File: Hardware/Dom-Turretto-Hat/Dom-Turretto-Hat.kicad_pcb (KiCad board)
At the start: 2 copper layers, 65 x 56 mm, 54 parts, among them J1 Raspberry_Pi_2_3, J2 Conn_Coaxial, J3 Barrel_Jack_Switch, J4 Conn_01x02, U1 CAT24C32WI-GT3, U2 MAX-M8Q, U3 LM22679TJ-5.0/NOPB, U4 LTC4451AV#TRMPBF, U5 LTC4451AV#TRMPBF, U6 LT1963AxST-3.3, U7 LTC4411ES5TRMPBF

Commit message: Fix XT60 connector
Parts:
- J4: footprint Connector_AMASS:AMASS_XT60-F_1x02_P7.20mm_Vertical -> Connector_AMASS:AMASS_XT60-M_1x02_P7.20mm_Vertical
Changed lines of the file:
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@@
     )
   )
-  (footprint "Connector_AMASS:AMASS_XT60-F_1x02_P7.20mm_Vertical" (layer "F.Cu")
+  (footprint "Connector_AMASS:AMASS_XT60-M_1x02_P7.20mm_Vertical" (layer "F.Cu")
     (at 151.5 121.9 -90)
     (descr "AMASS female XT60, through hole, vertical, https://www.tme.eu/Document/2d152ced3b7a446066e6c419d84bb460/XT60%20SPEC.pdf")
@@
       (effects (font (size 1 1) (thickness 0.15)))
     )
-    (fp_text value "Conn_01x02" (at 3.6 5.4 90) (layer "F.Fab")
+    (fp_text value "Conn_01x02" (at 3.6 5.4 -90) (layer "F.Fab")
       (effects (font (size 1 1) (thickness 0.15)))
     )
-    (fp_text user "${REFERENCE}" (at 3.6 0.05 90) (layer "F.Fab")
+    (fp_text user "${REFERENCE}" (at 3.6 0.05 -90) (layer "F.Fab")
       (effects (font (size 1 1) (thickness 0.15)))
     )
-    (fp_line (start 11.45 4.15) (end 11.45 -4.15) (layer "F.SilkS") (width 0.12))
-    (fp_line (start -1.4 -4.15) (end -4.25 -1.6) (layer "F.SilkS") (width 0.12))
-    (fp_line (start -4.25 -1.6) (end -4.25 1.55) (layer "F.SilkS") (width 0.12))
     (fp_line (start -1.4 4.15) (end 11.45 4.15) (layer "F.SilkS") (width 0.12))
     (fp_line (start 11.45 -4.15) (end -1.4 -4.15) (layer "F.SilkS") (width 0.12))
+    (fp_line (start -4.25 -1.6) (end -4.25 1.55) (layer "F.SilkS") (width 0.12))
+    (fp_line (start -1.4 -4.15) (end -4.25 -1.6) (layer "F.SilkS") (width 0.12))
     (fp_line (start -4.25 1.55) (end -1.4 4.15) (layer "F.SilkS") (width 0.12))
+    (fp_line (start 11.45 4.15) (end 11.45 -4.15) (layer "F.SilkS") (width 0.12))
+    (fp_line (start -4.65 1.85) (end -4.65 -1.85) (layer "F.CrtYd") (width 0.05))
+    (fp_line (start 11.85 -4.6) (end 11.85 4.6) (layer "F.CrtYd") (width 0.05))
+    (fp_line (start -4.65 -1.85) (end -1.6 -4.6) (layer "F.CrtYd") (width 0.05))
+    (fp_line (start -1.6 4.6) (end -4.65 1.85) (layer "F.CrtYd") (width 0.05))
     (fp_line (start -1.6 -4.6) (end 11.85 -4.6) (layer "F.CrtYd") (width 0.05))
-    (fp_line (start -4.65 -1.85) (end -1.6 -4.6) (layer "F.CrtYd") (width 0.05))
-    (fp_line (start 11.85 -4.6) (end 11.85 4.6) (layer "F.CrtYd") (width 0.05))
     (fp_line (start 11.85 4.6) (end -1.6 4.6) (layer "F.CrtYd") (width 0.05))
-    (fp_line (start -1.6 4.6) (end -4.65 1.85) (layer "F.CrtYd") (width 0.05))
-    (fp_line (start -4.65 1.85) (end -4.65 -1.85) (layer "F.CrtYd") (width 0.05))
     (fp_line (start -4.15 1.55) (end -1.4 4.05) (layer "F.Fab") (width 0.12))
-    (fp_line (start -4.15 -1.55) (end -4.15 1.55) (layer "F.Fab") (width 0.12))
     (fp_line (start -1.4 4.05) (end 11.35 4.05) (layer "F.Fab") (width 0.12))
     (fp_line (start 11.35 -4.05) (end -1.4 -4.05) (layer "F.Fab") (width 0.12))
+    (fp_line (start -4.15 -1.55) (end -4.15 1.55) (layer "F.Fab") (width 0.12))
     (fp_line (start 11.35 4.05) (end 11.35 -4.05) (layer "F.Fab") (width 0.12))
     (fp_line (start -1.4 -4.05) (end -4.15 -1.55) (layer "F.Fab") (width 0.12))
@@
     (pad "2" thru_hole circle (at 7.2 0 270) (size 6 6) (drill 4.5) (layers *.Cu *.Mask)
       (net 1 "GND") (pinfunction "Pin_2") (pintype "passive"))
-    (model "${KICAD6_3DMODEL_DIR}/Connector_AMASS.3dshapes/AMASS_XT60-F_1x02_P7.2mm_Vertical.wrl"
+    (model "${KICAD6_3DMODEL_DIR}/Connector_AMASS.3dshapes/AMASS_XT60-M_1x02_P7.2mm_Vertical.wrl"
       (offset (xyz 0 0 0))
       (scale (xyz 1 1 1))

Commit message: Updated schematic
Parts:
- removed C1: 10nF, Capacitor_SMD:C_0603_1608Metric
- removed J2: Conn_Coaxial, Connector_Coaxial:SMA_Molex_73251-1153_EdgeMount_Horizontal
- removed L1: 27nH, Inductor_SMD:L_0603_1608Metric
- removed R4: 10K, Resistor_SMD:R_0603_1608Metric
- removed R5: 10, Resistor_SMD:R_0603_1608Metric
- removed Stepper1, Stepper2: Conn_01x04_Male, Connector_PinHeader_2.54mm:PinHeader_1x04_P2.54mm_Vertical
- removed U2: MAX-M8Q, RF_GPS:ublox_MAX
- added StepperConnector1: Screw_Terminal_01x04, TerminalBlock_TE-Connectivity:TerminalBlock_TE_282834-4_1x04_P2.54mm_Horizontal, F.Cu at (175.2, 121.8)
- added StepperConnector2: Screw_Terminal_01x04, TerminalBlock_TE-Connectivity:TerminalBlock_TE_282834-4_1x04_P2.54mm_Horizontal, F.Cu at (175.0, 100.2)
- moved J3 3.64 mm to (135.7, 120.7)
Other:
- outline, holes or cut-outs redrawn

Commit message: Update components
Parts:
- removed U4, U5: LTC4451AV#TRMPBF, iclr:IC_LTC4451AV#TRMPBF
- added H5: MountingHole, MountingHole:MountingHole_2.7mm_M2.5, F.Cu at (173.0, 104.5)
- added H6: MountingHole, MountingHole:MountingHole_2.7mm_M2.5, F.Cu at (115.0, 104.5)
- added Q1: RSJ250P10TL, Package_TO_SOT_SMD:TO-263-3_TabPin2, F.Cu at (194.5, 95.8)
- added Q2: RSJ250P10TL, Package_TO_SOT_SMD:TO-263-3_TabPin2, F.Cu at (206.2, 115.5)
- added R4: 470k, Resistor_SMD:R_0603_1608Metric, F.Cu at (192.8, 103.2)
- added U2: LTC4412xS6, Package_TO_SOT_SMD:TSOT-23-6, F.Cu at (188.2, 104.2)
- J4: footprint Connector_AMASS:AMASS_XT60-M_1x02_P7.20mm_Vertical -> Connector_AMASS:AMASS_XT60-F_1x02_P7.20mm_Vertical
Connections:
- A1 pad 13: +3V3 -> +5V
- A1 pad 14: +3V3 -> +5V
- A1 pad 2: +3V3 -> +5V
- A2 pad 13: +3V3 -> +5V
- A2 pad 14: +3V3 -> +5V
- A2 pad 2: +3V3 -> +5V
- R_Opt1 pad 2: +3V3 -> +5V
- R_Opt2 pad 2: +3V3 -> +5V
- R_Opt3 pad 2: +3V3 -> +5V
- R_Opt4 pad 2: +3V3 -> +5V

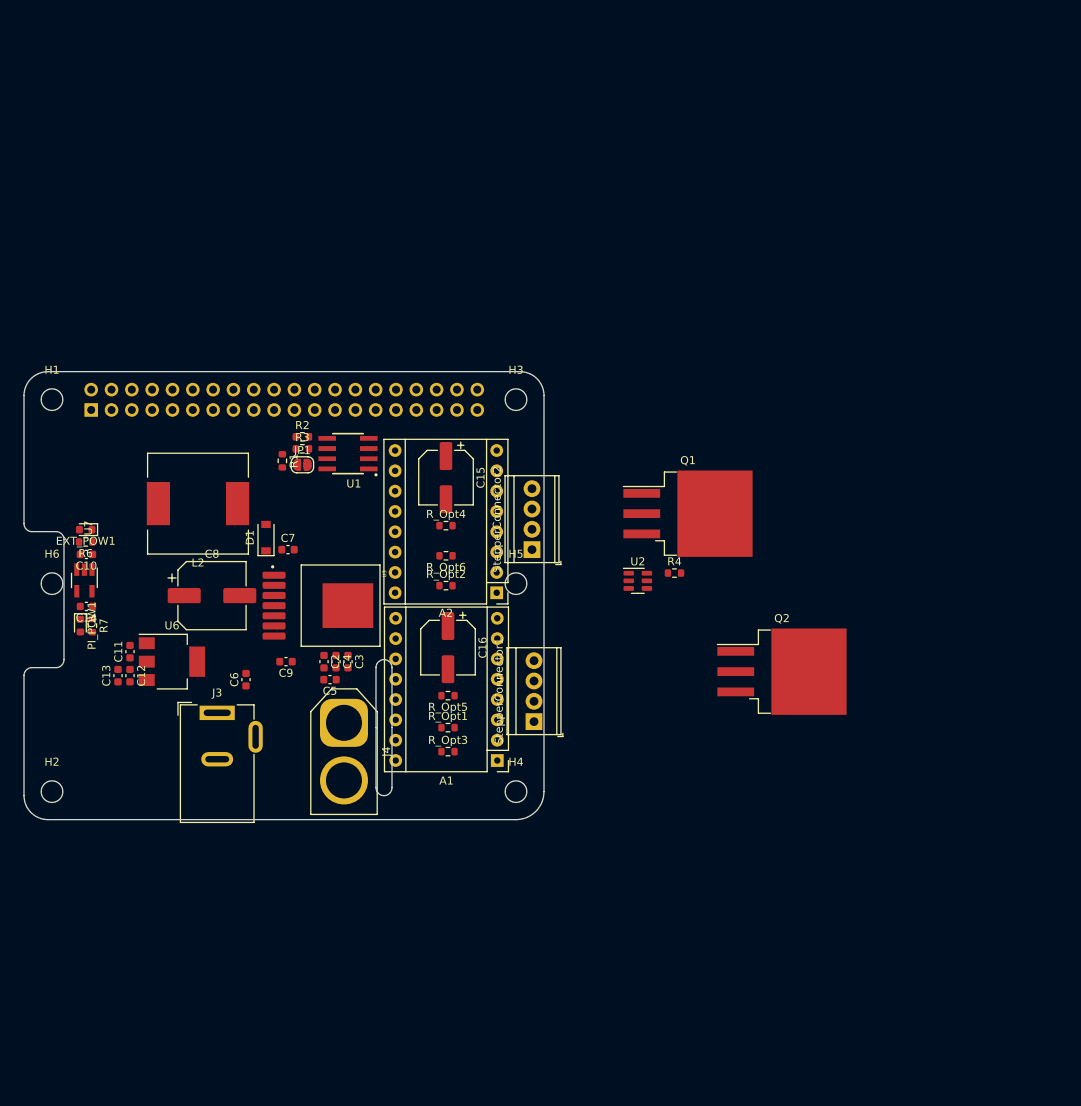
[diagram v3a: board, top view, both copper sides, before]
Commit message: Fix power circuitry values
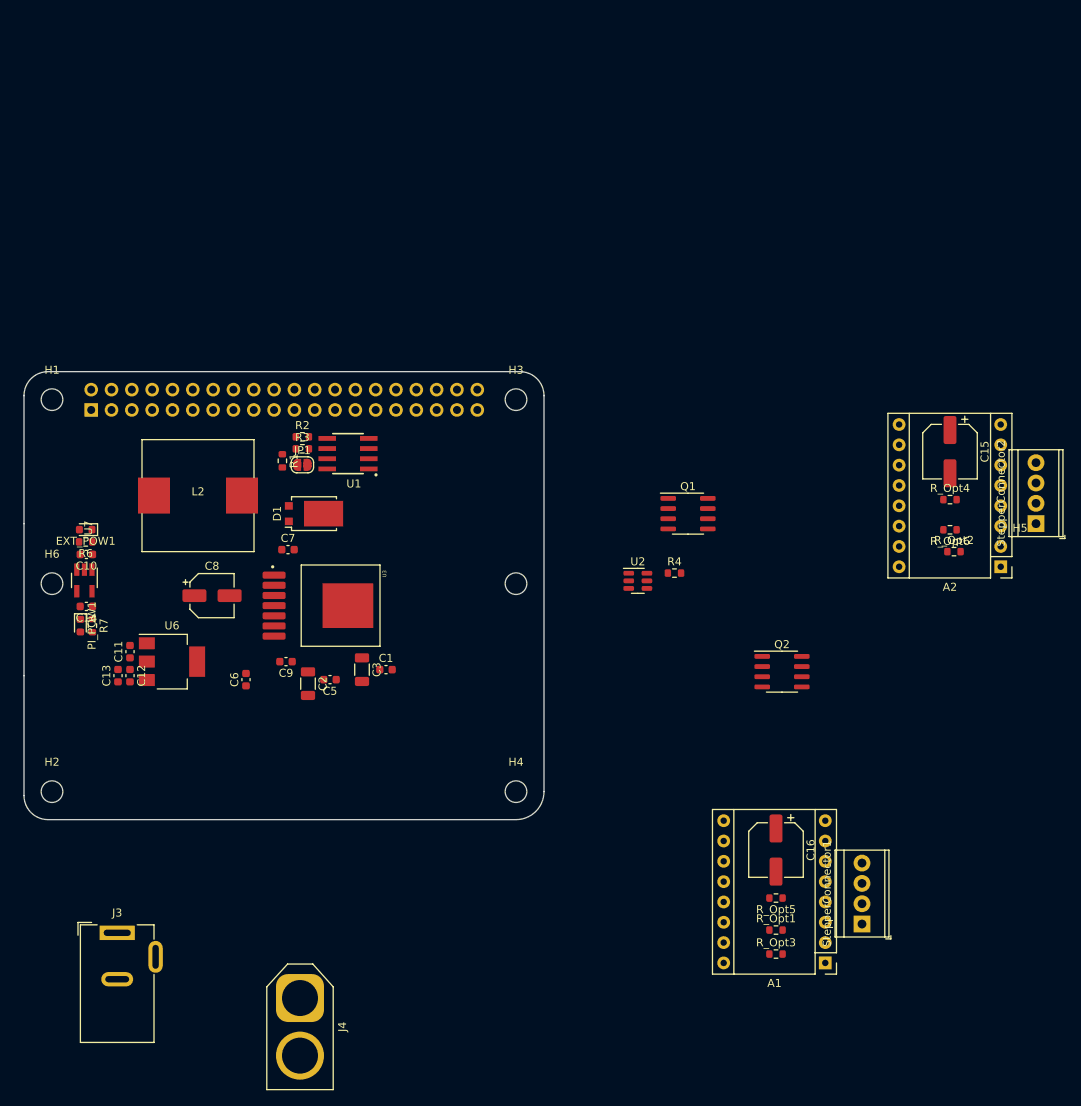
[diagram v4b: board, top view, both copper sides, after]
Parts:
- removed C4: 6.8uF, Capacitor_SMD:C_0603_1608Metric
- added C1: 1uF, Capacitor_SMD:C_0603_1608Metric, F.Cu at (156.8, 115.2)
- C2: value 22uF -> 10uF; footprint Capacitor_SMD:C_0603_1608Metric -> Capacitor_SMD:C_1206_3216Metric
- C3: value 6.8uF -> 10uF; footprint Capacitor_SMD:C_0603_1608Metric -> Capacitor_SMD:C_1206_3216Metric
- C8: value 180uF -> 100uF; footprint Capacitor_SMD:CP_Elec_8x11.9 -> Capacitor_SMD:CP_Elec_5x5.9
- D1: value D_Schottky -> DST1550S; footprint Diode_SMD:D_SOD-123 -> Package_TO_SOT_SMD:TO-277B
- L2: value 29uH -> 8.2uH; footprint Inductor_SMD:L_12x12mm_H8mm -> iclr:Bourns_SRP1270
- Q1, Q2: value RSJ250P10TL -> SI4143DY-T1-GE3; footprint Package_TO_SOT_SMD:TO-263-3_TabPin2 -> Package_SO:SOIC-8_3.9x4.9mm_P1.27mm
- moved R_Opt2 63.6 mm to (227.8, 100.5)
- moved A2 63.1 mm to (233.6, 102.4)
- moved C15 63.1 mm to (227.2, 88.0)
- moved R_Opt4 63.1 mm to (227.2, 94.0)
- moved R_Opt6 63.1 mm to (227.2, 97.8)
- moved StepperConnector2 63.1 mm to (238.0, 97.0)
- moved C16 48.2 mm to (205.5, 137.8)
- moved R_Opt1 48.2 mm to (205.5, 147.8)
- moved R_Opt3 48.2 mm to (205.5, 150.8)
- moved R_Opt5 48.2 mm to (205.5, 143.8)
- moved StepperConnector1 48.2 mm to (216.2, 147.1)
- moved A1 48.2 mm to (211.7, 151.9)
- moved J4 34.8 mm to (146.0, 156.3)
- moved J3 30.2 mm to (123.2, 148.2)
- moved D1 6.71 mm to (147.8, 95.8)
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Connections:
- A1 pad 13: +5V -> +3V3
- A1 pad 14: +5V -> +3V3
- A1 pad 2: +5V -> +3V3
- A2 pad 13: +5V -> +3V3
- A2 pad 14: +5V -> +3V3
- A2 pad 2: +5V -> +3V3
- D1 pad 1: Net-(C7-Pad2) -> GND
- Q1 pad 1: Net-(Q1-Pad1) -> Net-(C5-Pad1)
- Q1 pad 3: VCC -> Net-(C5-Pad1)
- Q2 pad 1: Net-(Q2-Pad1) -> Net-(C6-Pad1)
- Q2 pad 3: VCC -> Net-(C6-Pad1)
- R4 pad 1: Net-(Q2-Pad1) -> Net-(R4-Pad1)
- R_Opt1 pad 2: +5V -> +3V3
- R_Opt2 pad 2: +5V -> +3V3
- R_Opt3 pad 2: +5V -> +3V3
- R_Opt4 pad 2: +5V -> +3V3
- U2 pad 4: Net-(Q2-Pad1) -> Net-(R4-Pad1)
- U2 pad 5: Net-(Q1-Pad1) -> Net-(U2-Pad5)
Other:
- outline, holes or cut-outs redrawn

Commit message: Remove 3.3V regulator and use pi power for logic
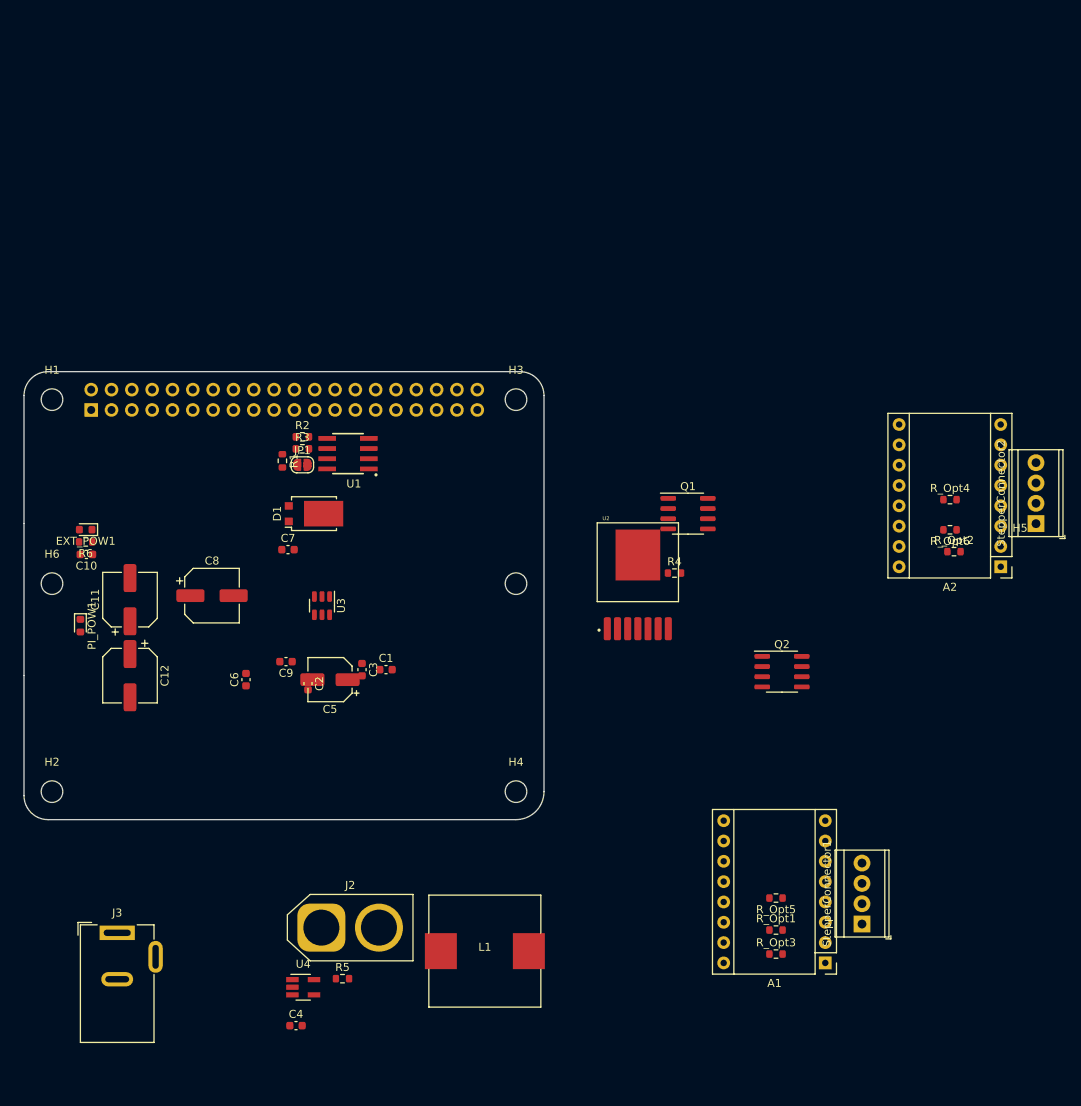
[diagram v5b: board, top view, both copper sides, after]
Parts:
- removed C13: 100nF, Capacitor_SMD:C_0603_1608Metric
- removed C14: 4.7uF, Capacitor_SMD:C_0603_1608Metric
- removed C15, C16: 47uF, Capacitor_SMD:CP_Elec_6.3x7.7
- removed J4: Conn_01x02, Connector_AMASS:AMASS_XT60-F_1x02_P7.20mm_Vertical
- removed L2: 8.2uH, iclr:Bourns_SRP1270
- removed R7: 1k, Resistor_SMD:R_0603_1608Metric
- removed U6: LT1963AxST-3.3, Package_TO_SOT_SMD:SOT-223-3_TabPin2
- removed U7: LTC4411ES5TRMPBF, Package_TO_SOT_SMD:SOT-23-5_HandSoldering
- added C4: 10nF, Capacitor_SMD:C_0603_1608Metric, F.Cu at (145.5, 159.8)
- added J2: Conn_01x02, Connector_AMASS:AMASS_XT60-F_1x02_P7.20mm_Vertical, F.Cu at (148.7, 147.5)
- added L1: 8.2uH, iclr:Bourns_SRP1270, F.Cu at (169.1, 150.4)
- added R5: 1k, Resistor_SMD:R_0603_1608Metric, F.Cu at (151.3, 153.9)
- added U4: LTC4411ES5TRMPBF, Package_TO_SOT_SMD:SOT-23-5_HandSoldering, F.Cu at (146.4, 154.9)
- C1: value 1uF -> 10uF
- C10: value 1uF -> 4.7uF
- C11, C12: value 10uF -> 47uF; footprint Capacitor_SMD:C_0603_1608Metric -> Capacitor_SMD:CP_Elec_6.3x7.7
- C2: footprint Capacitor_SMD:C_1206_3216Metric -> Capacitor_SMD:C_0603_1608Metric
- C3: value 10uF -> 1uF; footprint Capacitor_SMD:C_1206_3216Metric -> Capacitor_SMD:C_0603_1608Metric
- C5: value 0.1uF -> 100uF; footprint Capacitor_SMD:C_0603_1608Metric -> Capacitor_SMD:CP_Elec_5x5.9
- C7: value 10nF -> 0.1uF
- C8: value 100uF -> 47uF; footprint Capacitor_SMD:CP_Elec_5x5.9 -> Capacitor_SMD:CP_Elec_6.3x7.7
- C9: value 10uF -> 1uF
- U2: value LTC4412xS6 -> LM22679TJ-5.0/NOPB; footprint Package_TO_SOT_SMD:TSOT-23-6 -> iclr:TO127P1401X200-7N
- U3: value LM22679TJ-5.0/NOPB -> LTC4412xS6; footprint iclr:TO127P1401X200-7N -> Package_TO_SOT_SMD:TSOT-23-6
- moved C11 6.50 mm to (124.8, 106.5)
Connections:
- C10 pad 1: /Power/5V_out -> +5V
- C11 pad 1: GND -> VCC
- C11 pad 2: +5V -> GND
- C12 pad 1: GND -> VCC
- C12 pad 2: +3V3 -> GND
- C5 pad 1: Net-(C5-Pad1) -> /Power/5V_out
- C7 pad 2: Net-(C7-Pad2) -> GND
- C8 pad 1: /Power/5V_out -> VCC
- C9 pad 1: VCC -> /Power/5V_out
- D1 pad 3: Net-(C7-Pad2) -> Net-(C4-Pad2)
- J1 pad 1: unconnected-(J1-Pad1) -> +3V3
- J1 pad 17: unconnected-(J1-Pad17) -> +3V3
- J3 pad 1: Net-(C6-Pad1) -> Net-(C7-Pad1)
- Q1 pad 1: Net-(C5-Pad1) -> Net-(C6-Pad1)
- Q1 pad 2: Net-(C5-Pad1) -> Net-(C6-Pad1)
- Q1 pad 3: Net-(C5-Pad1) -> Net-(C6-Pad1)
- Q1 pad 4: Net-(U2-Pad5) -> Net-(Q1-Pad4)
- Q2 pad 1: Net-(C6-Pad1) -> Net-(C7-Pad1)
- Q2 pad 2: Net-(C6-Pad1) -> Net-(C7-Pad1)
- Q2 pad 3: Net-(C6-Pad1) -> Net-(C7-Pad1)
- Q2 pad 4: Net-(R4-Pad1) -> Net-(Q2-Pad4)
- R4 pad 1: Net-(R4-Pad1) -> Net-(Q2-Pad4)
- R6 pad 1: /Power/5V_out -> +5V
- R6 pad 2: Net-(EXT_POW1-Pad2) -> Net-(PI_POW1-Pad2)
- U2 pad 1: Net-(C5-Pad1) -> Net-(C4-Pad2)
- U2 pad 2: GND -> VCC
- U2 pad 3: GND -> Net-(C4-Pad1)
- U2 pad 4: Net-(R4-Pad1) -> GND
- U2 pad 5: Net-(U2-Pad5) -> unconnected-(U2-Pad5)
- U2 pad 6: VCC -> /Power/5V_out
- U3 pad 1: Net-(C7-Pad2) -> Net-(C6-Pad1)
- U3 pad 2: VCC -> GND
- U3 pad 3: Net-(C7-Pad1) -> GND
- U3 pad 4: GND -> Net-(Q2-Pad4)
- U3 pad 5: unconnected-(U3-Pad5) -> Net-(Q1-Pad4)
- U3 pad 6: /Power/5V_out -> VCC

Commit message: Did initial laying out of components
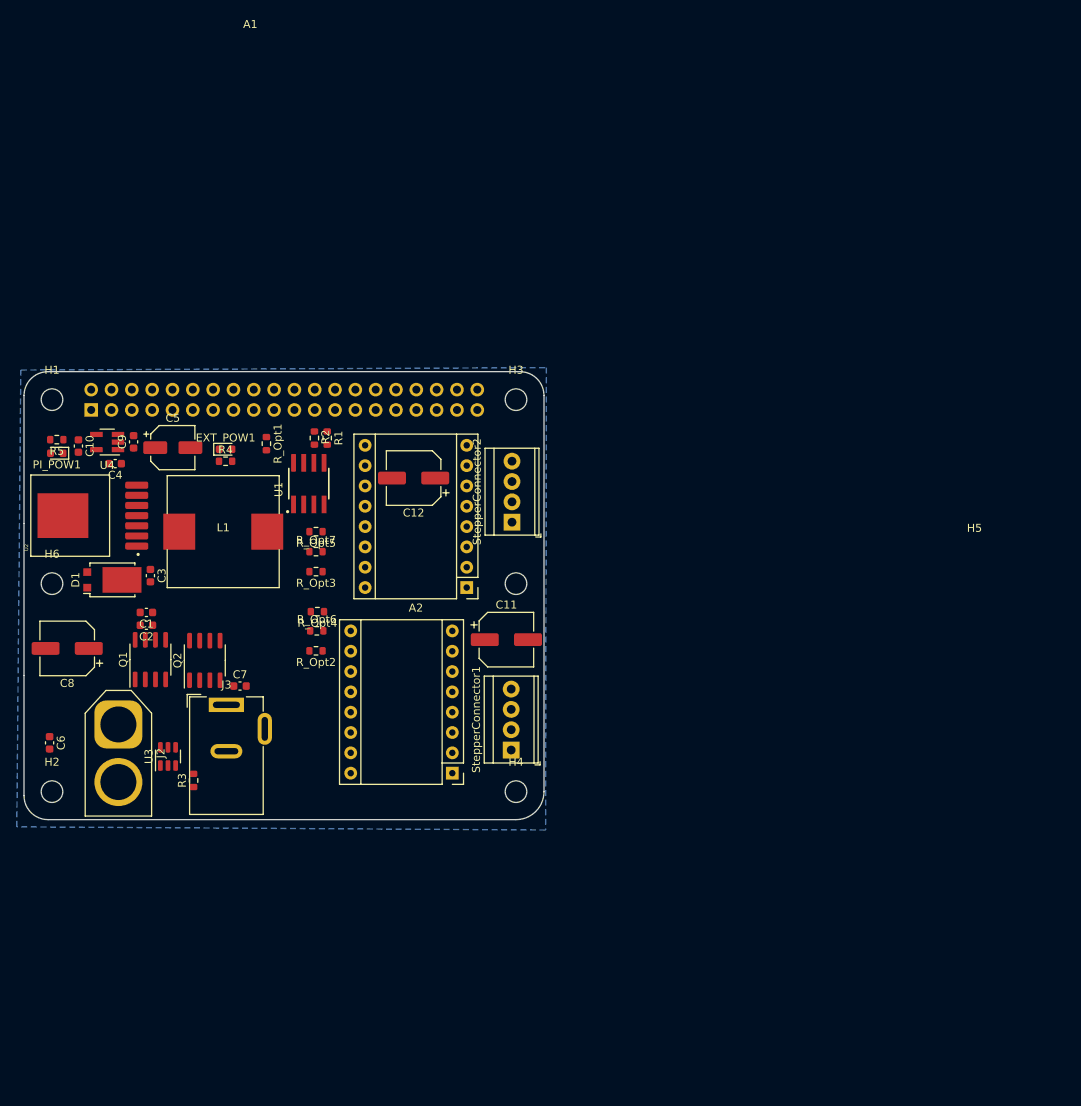
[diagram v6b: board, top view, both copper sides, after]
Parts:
- removed JP1: SolderJumper_2_Open, Jumper:SolderJumper-2_P1.3mm_Open_RoundedPad1.0x1.5mm
- removed R6: 1k, Resistor_SMD:R_0603_1608Metric
- added R_Opt7: 10k, Resistor_SMD:R_0603_1608Metric, F.Cu at (148.0, 100.5)
- R1: value 10k -> 3.9k
- R3: value 3.9k -> 470k
- R4: value 470k -> 1k
- moved R_Opt1 88.1 mm to (141.8, 87.0), turned to -90 degrees
- moved R_Opt2 80.7 mm to (148.0, 112.9), turned to 180 degrees
- moved R_Opt4 80.3 mm to (148.2, 108.0), turned to 180 degrees
- moved R_Opt6 80.2 mm to (148.1, 110.4), turned to 0 degrees
- moved R5 76.3 mm to (115.6, 86.5), turned to 180 degrees
- moved R_Opt3 74.8 mm to (148.0, 103.0), turned to 180 degrees
- moved C4 73.8 mm to (122.9, 89.5), turned to 180 degrees
- moved R_Opt5 73.5 mm to (148.0, 98.0)
- moved U4 72.4 mm to (121.9, 86.8), turned to 180 degrees
- moved Q2 72.2 mm to (134.1, 114.1), turned to 90 degrees
- moved Q1 69.6 mm to (127.3, 114.0), turned to 90 degrees
- moved U2 69.1 mm to (119.6, 96.0), turned to 90 degrees
- moved A2 66.8 mm to (166.8, 105.0)
- moved StepperConnector2 65.5 mm to (172.5, 96.8)
- moved L1 61.8 mm to (136.4, 98.0)
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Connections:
- R1 pad 2: Net-(JP1-Pad1) -> /ID_SDA_EEPROM
- R2 pad 2: /ID_SDA_EEPROM -> /ID_SCL_EEPROM
- R3 pad 1: +3V3 -> Net-(Q2-Pad4)
- R3 pad 2: /ID_SCL_EEPROM -> VCC
- R4 pad 1: Net-(Q2-Pad4) -> /Power/5V_out
- R4 pad 2: VCC -> Net-(EXT_POW1-Pad2)
- R5 pad 1: /Power/5V_out -> +5V
- R5 pad 2: Net-(EXT_POW1-Pad2) -> Net-(PI_POW1-Pad2)
- R_Opt1 pad 1: Net-(A1-Pad12) -> +3V3
- R_Opt1 pad 2: +3V3 -> Net-(R_Opt1-Pad2)
- R_Opt2 pad 1: Net-(A2-Pad12) -> Net-(A1-Pad12)
- R_Opt3 pad 1: Net-(A1-Pad10) -> Net-(A2-Pad12)
- R_Opt4 pad 1: Net-(A2-Pad10) -> Net-(A1-Pad10)
- R_Opt5 pad 1: GND -> Net-(A2-Pad10)
- R_Opt5 pad 2: Net-(A1-Pad11) -> +3V3
- R_Opt6 pad 2: Net-(A2-Pad11) -> Net-(A1-Pad11)
- U1 pad 7: Net-(JP1-Pad2) -> Net-(R_Opt1-Pad2)
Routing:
- added copper zone on B.Cu, net GND
